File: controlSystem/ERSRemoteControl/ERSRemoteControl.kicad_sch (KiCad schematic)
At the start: 54 parts, among them J1 USB_C_Receptacle_USB2.0_14P, J2 0022-232041, J3 Conn_01x06, J4 00222-32051, J5 0022-232021, J6 0022-232021, SW1 SW_SPDT, SW2 SW_Push, SW3 SW_Push, SW4 SW_Push, SW5 SW_Push, SW6 SW_Push, SW7 SW_Push, U1 TPS63070, U2 ESP32-S3-WROOM-1, U3 TCAN330

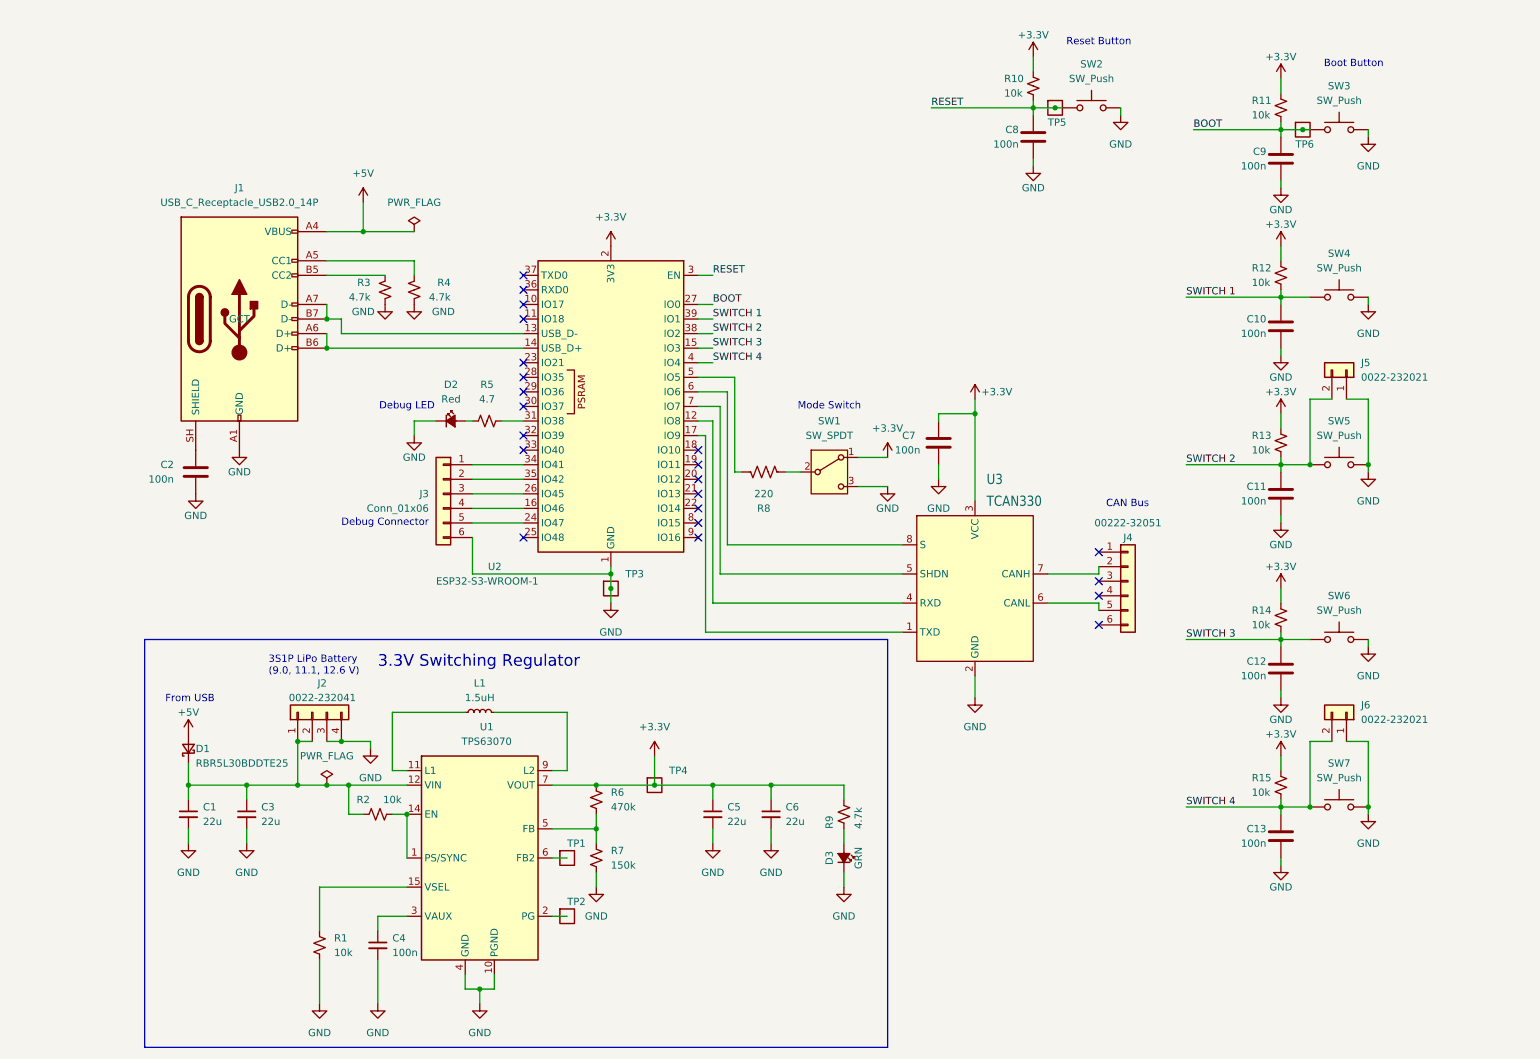
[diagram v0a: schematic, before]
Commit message: Removed CAN stuff and replaced with serial
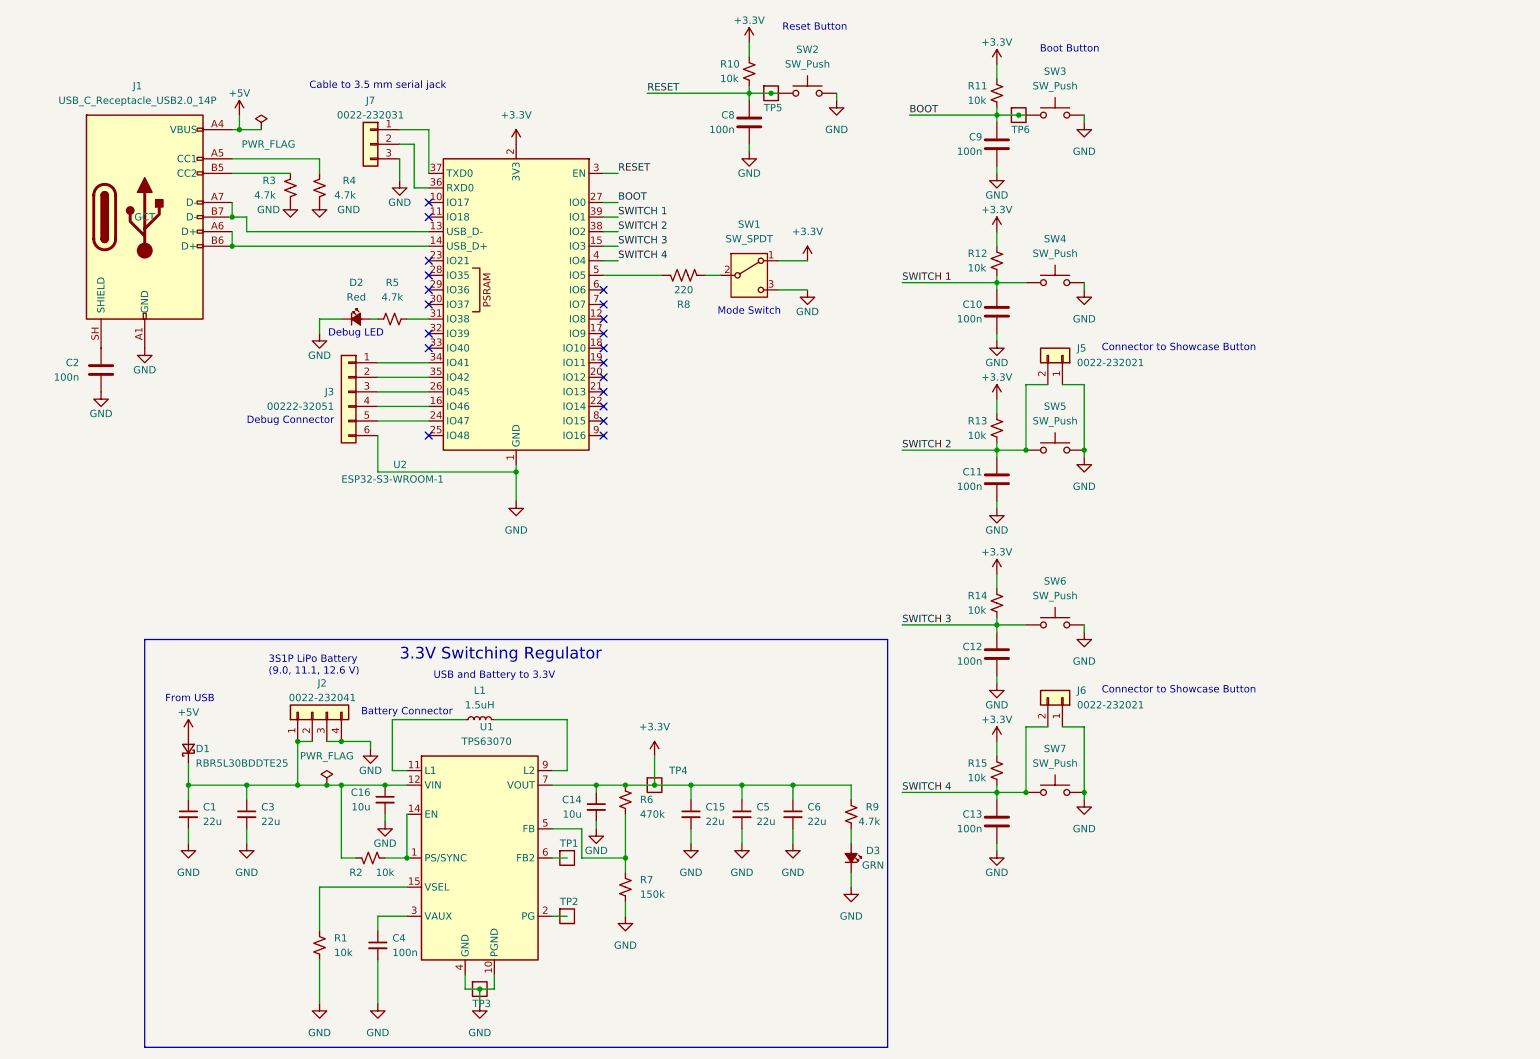
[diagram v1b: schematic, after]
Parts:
- removed C7: 100n, Capacitor_SMD:C_0603_1608Metric, symbol Device:C
- removed J4: 00222-32051, Connector_Molex:Molex_KK-254_AE-6410-06A_1x06_P2.54mm_Vertical, symbol Connector_Generic:Conn_01x06
- removed U3: TCAN330, psas-footprints:SOT23-8, symbol U-TI-TCAN330-can-transciever:TCAN330
- added C14, C16: 10u, Capacitor_SMD:C_0603_1608Metric, symbol Device:C_Small
- added C15: 22u, Capacitor_SMD:C_0805_2012Metric, symbol Device:C_Small
- added J7: 0022-232031, Connector_Molex:Molex_KK-254_AE-6410-03A_1x03_P2.54mm_Vertical, symbol Connector_Generic:Conn_01x03
- C1, C3, C5, C6: footprint Capacitor_SMD:C_0603_1608Metric -> Capacitor_SMD:C_0805_2012Metric
- D2: DPN (none) -> 732-4979-1-ND; DST (none) -> DigiKey; MFR (none) -> Wurth; MPN (none) -> 150060SS75000
- J3: value Conn_01x06 -> 00222-32051; DPN (none) -> WM4204-ND; DST (none) -> DigiKey; MFR (none) -> Molex; MPN (none) -> 22232061
- R5: value 4.7 -> 4.7k; DPN (none) -> 311-4.70KHRCT-ND; DST (none) -> DigiKey; MFR (none) -> Yageo; MPN (none) -> RC0603FR-074K7L
- R8: DPN (none) -> 311-220GRCT-ND; DST (none) -> DigiKey; MFR (none) -> Yageo; MPN (none) -> RC0603JR-07220RL
- SW1: DPN (none) -> 401-1999-1-ND; DST (none) -> DigiKey; MFR (none) -> C&K; MPN (none) -> JS102011SAQN
- SW2, SW3, SW4, SW5, SW6, SW7: DST (none) -> DigiKey; MFR Omron Electronics Inc-EMC Div -> Arata
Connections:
- net +3.3V: now also C14.1, C15.1
- net GND: now also C14.2, C15.2, C16.2, J7.3 (Pin_3)
- net at C1.1, C3.1, D1.1 (K)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: now also C16.1
- net at U2.36 (RXD0): now also J7.2 (Pin_2)
- net at U2.37 (TXD0): now also J7.1 (Pin_1)
- no-connect marks 22 -> 20
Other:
- note added: "Battery Connector"
- note added: "Cable to 3.5 mm serial jack"
- note added: "Connector to Showcase Button"
- note added: "USB and Battery to 3.3V"
- note removed: "CAN Bus"
- moved on the sheet: C10, C11, C12, C13, C2, C5, C6, C8, C9, D2, D3, J1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

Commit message: More changes to layout to make it cleaner
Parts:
- removed J3: 00222-32051, Connector_Molex:Molex_KK-254_AE-6410-06A_1x06_P2.54mm_Vertical, symbol Connector_Generic:Conn_01x06
- added TP7, TP8: Test-Point, psas-footprints:TP-through-hole-1X01, symbol psas-testpoint:Test-Point
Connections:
- net at U2.34 (IO41): now also TP7.1
- net at U2.35 (IO42): now also TP8.1
- no-connect marks 20 -> 19
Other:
- note removed: "Debug Connector"

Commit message: Replaced components in BOM
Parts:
- C1, C15, C3, C5, C6: DPN 445-14428-1-ND -> 490-GRT21BC81C226ME13LCT-ND; MPN C2012X5R1V226M125AC -> GRT21BC81C226ME13L
- C14, C16: footprint Capacitor_SMD:C_0603_1608Metric -> Capacitor_SMD:C_0805_2012Metric; DPN 445-14428-1-ND -> 490-GRT21BC71E106KE13KCT-ND; MPN C2012X5R1V226M125AC -> GRT21BC71E106KE13K
- R3, R4, R5, R9: DPN 311-4.70KHRCT-ND -> RMCF0603FT4K70CT-ND; MFR Yageo -> Stackpole Electronics Inc.; MPN RC0603FR-074K7L -> RMCF0603FT4K70
- R6: DPN 311-470KHRCT-ND -> RMCF0603FT470KCT-ND; MFR Yageo -> Stackpole Electronics Inc.; MPN RC0603FR-07470KL -> RMCF0603FT470K
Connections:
- no-connect marks 19 -> 23
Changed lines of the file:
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@@
 	)
 	(no_connect
+		(at 87.63 86.36)
+	)
+	(no_connect
 		(at 118.11 60.96)
 	)
@@
 	)
 	(no_connect
+		(at 87.63 83.82)
+	)
+	(no_connect
 		(at 118.11 66.04)
 	)
@@
 	)
 	(no_connect
+		(at 87.63 78.74)
+	)
+	(no_connect
 		(at 87.63 68.58)
 	)
@@
 	)
 	(no_connect
+		(at 87.63 81.28)
+	)
+	(no_connect
 		(at 87.63 45.72)
 	)
@@
 			)
 		)
-		(property "DPN" "311-470KHRCT-ND"
+		(property "DPN" "RMCF0603FT470KCT-ND"
 			(at 121.92 149.86 0)
 			(hide yes)
@@
 			)
 		)
-		(property "MFR" "Yageo"
+		(property "MFR" "Stackpole Electronics Inc."
 			(at 121.92 149.86 0)
 			(hide yes)
@@
 			)
 		)
-		(property "MPN" "RC0603FR-07470KL"
+		(property "MPN" "RMCF0603FT470K"
 			(at 121.92 149.86 0)
 			(hide yes)
@@
 			)
 		)
-		(property "MFR" "Yageo"
+		(property "MFR" "Stackpole Electronics Inc."
 			(at 81.28 66.04 90)
 			(hide yes)
@@
 			)
 		)
-		(property "MPN" "RC0603FR-074K7L"
+		(property "MPN" "RMCF0603FT4K70"
 			(at 81.28 66.04 90)
 			(hide yes)
@@
 			)
 		)
-		(property "DPN" "311-4.70KHRCT-ND"
+		(property "DPN" "RMCF0603FT4K70CT-ND"
 			(at 81.28 66.04 90)
 			(hide yes)
@@
 			)
 		)
-		(property "MFR" "Yageo"
+		(property "MFR" "Stackpole Electronics Inc."
 			(at 63.5 43.18 0)
 			(hide yes)
@@
 			)
 		)
-		(property "MPN" "RC0603FR-074K7L"
+		(property "MPN" "RMCF0603FT4K70"
 			(at 63.5 43.18 0)
 			(hide yes)
@@
 			)
 		)
-		(property "DPN" "311-4.70KHRCT-ND"
+		(property "DPN" "RMCF0603FT4K70CT-ND"
 			(at 63.5 43.18 0)
 			(hide yes)
@@
 			)
 		)
-		(property "DPN" "445-14428-1-ND"
+		(property "DPN" "490-GRT21BC81C226ME13LCT-ND"
 			(at 55.88 152.4 0)
 			(hide yes)
@@
 			)
 		)
-		(property "MPN" "C2012X5R1V226M125AC"
+		(property "MPN" "GRT21BC81C226ME13L"
 			(at 55.88 152.4 0)
 			(hide yes)
@@
 			)
 		)
-		(property "MPN" "C2012X5R1V226M125AC"
+		(property "MPN" "GRT21BC81C226ME13L"
 			(at 142.24 152.4 0)
 			(hide yes)
@@
 			)
 		)
-		(property "DPN" "445-14428-1-ND"
+		(property "DPN" "490-GRT21BC81C226ME13LCT-ND"
 			(at 142.24 152.4 0)
 			(hide yes)
@@
 			)
 		)
-		(property "DPN" "311-4.70KHRCT-ND"
+		(property "DPN" "RMCF0603FT4K70CT-ND"
 			(at 161.29 152.4 0)
 			(hide yes)
@@
 			)
 		)
-		(property "MFR" "Yageo"
+		(property "MFR" "Stackpole Electronics Inc."
 			(at 161.29 152.4 0)
 			(hide yes)
@@
 			)
 		)
-		(property "MPN" "RC0603FR-074K7L"
+		(property "MPN" "RMCF0603FT4K70"
 			(at 161.29 152.4 0)
 			(hide yes)
@@
 			)
 		)
-		(property "MPN" "C2012X5R1V226M125AC"
+		(property "MPN" "GRT21BC81C226ME13L"
 			(at 151.13 152.4 0)
 			(hide yes)
@@
 			)
 		)
-		(property "DPN" "445-14428-1-ND"
+		(property "DPN" "490-GRT21BC81C226ME13LCT-ND"
 			(at 151.13 152.4 0)
 			(hide yes)
@@
 			)
 		)
-		(property "MFR" "Yageo"
+		(property "MFR" "Stackpole Electronics Inc."
 			(at 68.58 43.18 0)
 			(hide yes)
@@
 			)
 		)
-		(property "MPN" "RC0603FR-074K7L"
+		(property "MPN" "RMCF0603FT4K70"
 			(at 68.58 43.18 0)
 			(hide yes)
@@
 			)
 		)
-		(property "DPN" "311-4.70KHRCT-ND"
+		(property "DPN" "RMCF0603FT4K70CT-ND"
 			(at 68.58 43.18 0)
 			(hide yes)
@@
 			)
 		)
-		(property "DPN" "445-14428-1-ND"
+		(property "DPN" "490-GRT21BC81C226ME13LCT-ND"
 			(at 45.72 152.4 0)
 			(hide yes)
@@
 			)
 		)
-		(property "MPN" "C2012X5R1V226M125AC"
+		(property "MPN" "GRT21BC81C226ME13L"
 			(at 45.72 152.4 0)
 			(hide yes)
@@
 			)
 		)
-		(property "Footprint" "Capacitor_SMD:C_0603_1608Metric"
+		(property "Footprint" "Capacitor_SMD:C_0805_2012Metric"
 			(at 80.01 149.86 0)
 			(hide yes)
@@
 			)
 		)
-		(property "MPN" "C2012X5R1V226M125AC"
+		(property "MPN" "GRT21BC71E106KE13K"
 			(at 80.01 149.86 0)
 			(hide yes)
@@
 			)
 		)
-		(property "DPN" "445-14428-1-ND"
+		(property "DPN" "490-GRT21BC71E106KE13KCT-ND"
 			(at 80.01 149.86 0)
 			(hide yes)
@@
 			)
 		)
-		(property "MPN" "C2012X5R1V226M125AC"
+		(property "MPN" "GRT21BC81C226ME13L"
 			(at 133.35 152.4 0)
 			(hide yes)
@@
 			)
 		)
-		(property "DPN" "445-14428-1-ND"
+		(property "DPN" "490-GRT21BC81C226ME13LCT-ND"
 			(at 133.35 152.4 0)
 			(hide yes)
@@
 			)
 		)
-		(property "Footprint" "Capacitor_SMD:C_0603_1608Metric"
+		(property "Footprint" "Capacitor_SMD:C_0805_2012Metric"
 			(at 116.84 151.13 0)
 			(hide yes)
@@
 			)
 		)
-		(property "MPN" "C2012X5R1V226M125AC"
+		(property "MPN" "GRT21BC71E106KE13K"
 			(at 116.84 151.13 0)
 			(hide yes)
@@
 			)
 		)
-		(property "DPN" "445-14428-1-ND"
+		(property "DPN" "490-GRT21BC71E106KE13KCT-ND"
 			(at 116.84 151.13 0)
 			(hide yes)

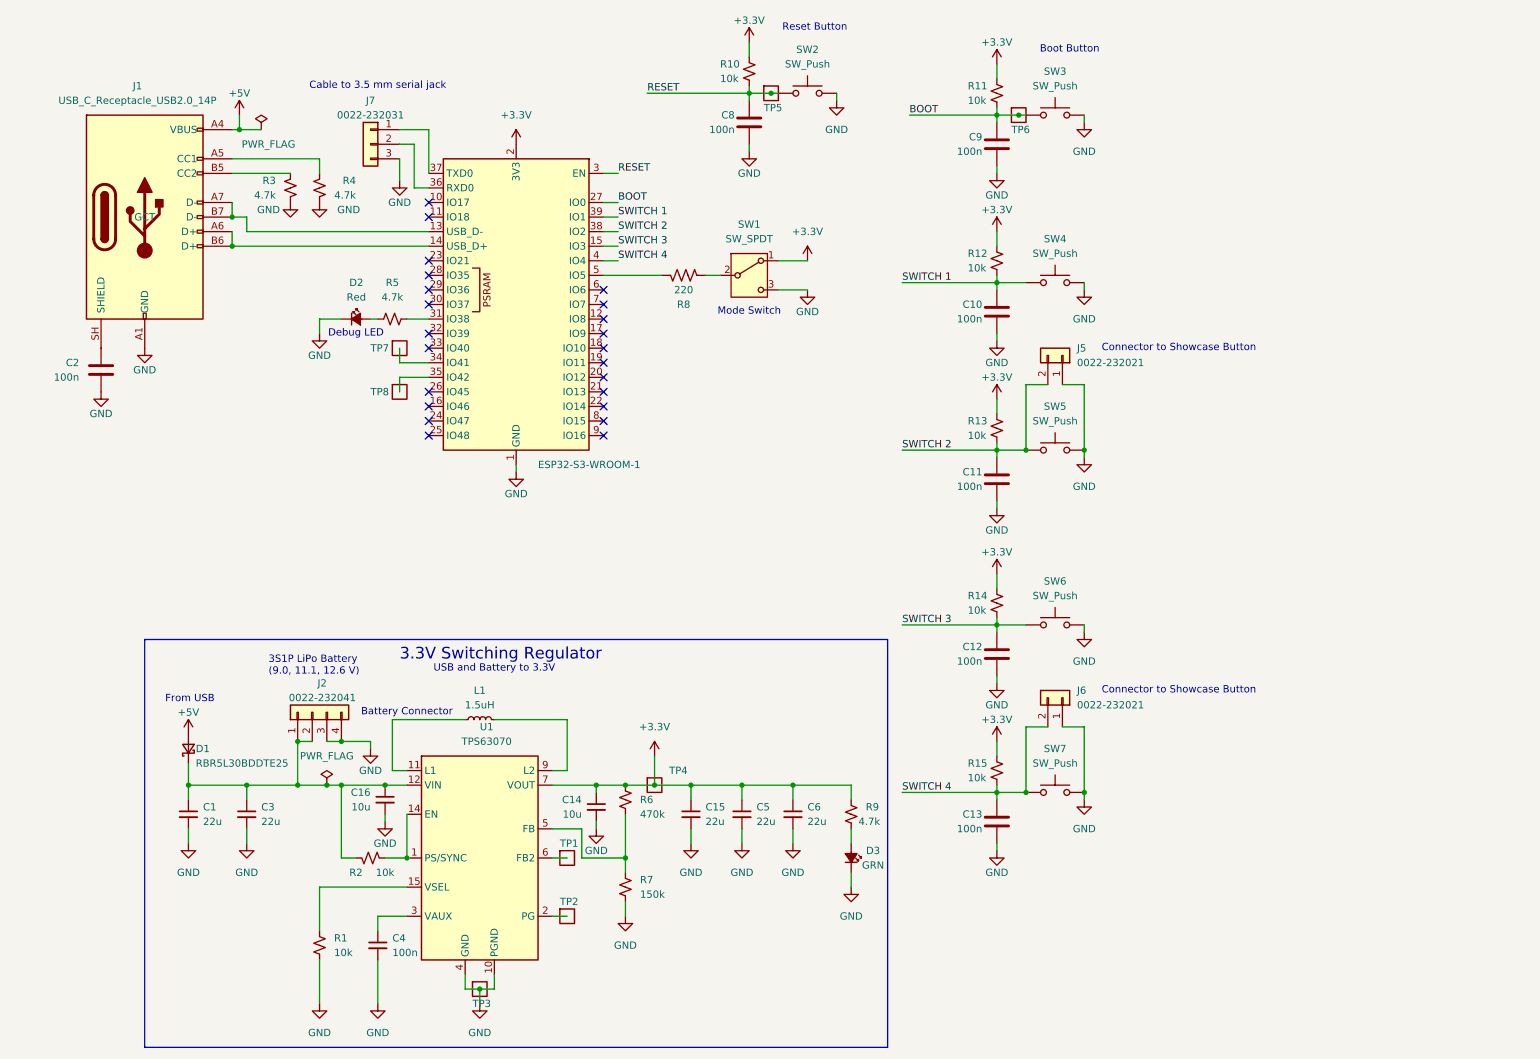
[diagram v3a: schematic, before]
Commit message: Removed mode switch cleaned up traces, minimum trace size to .3 mm
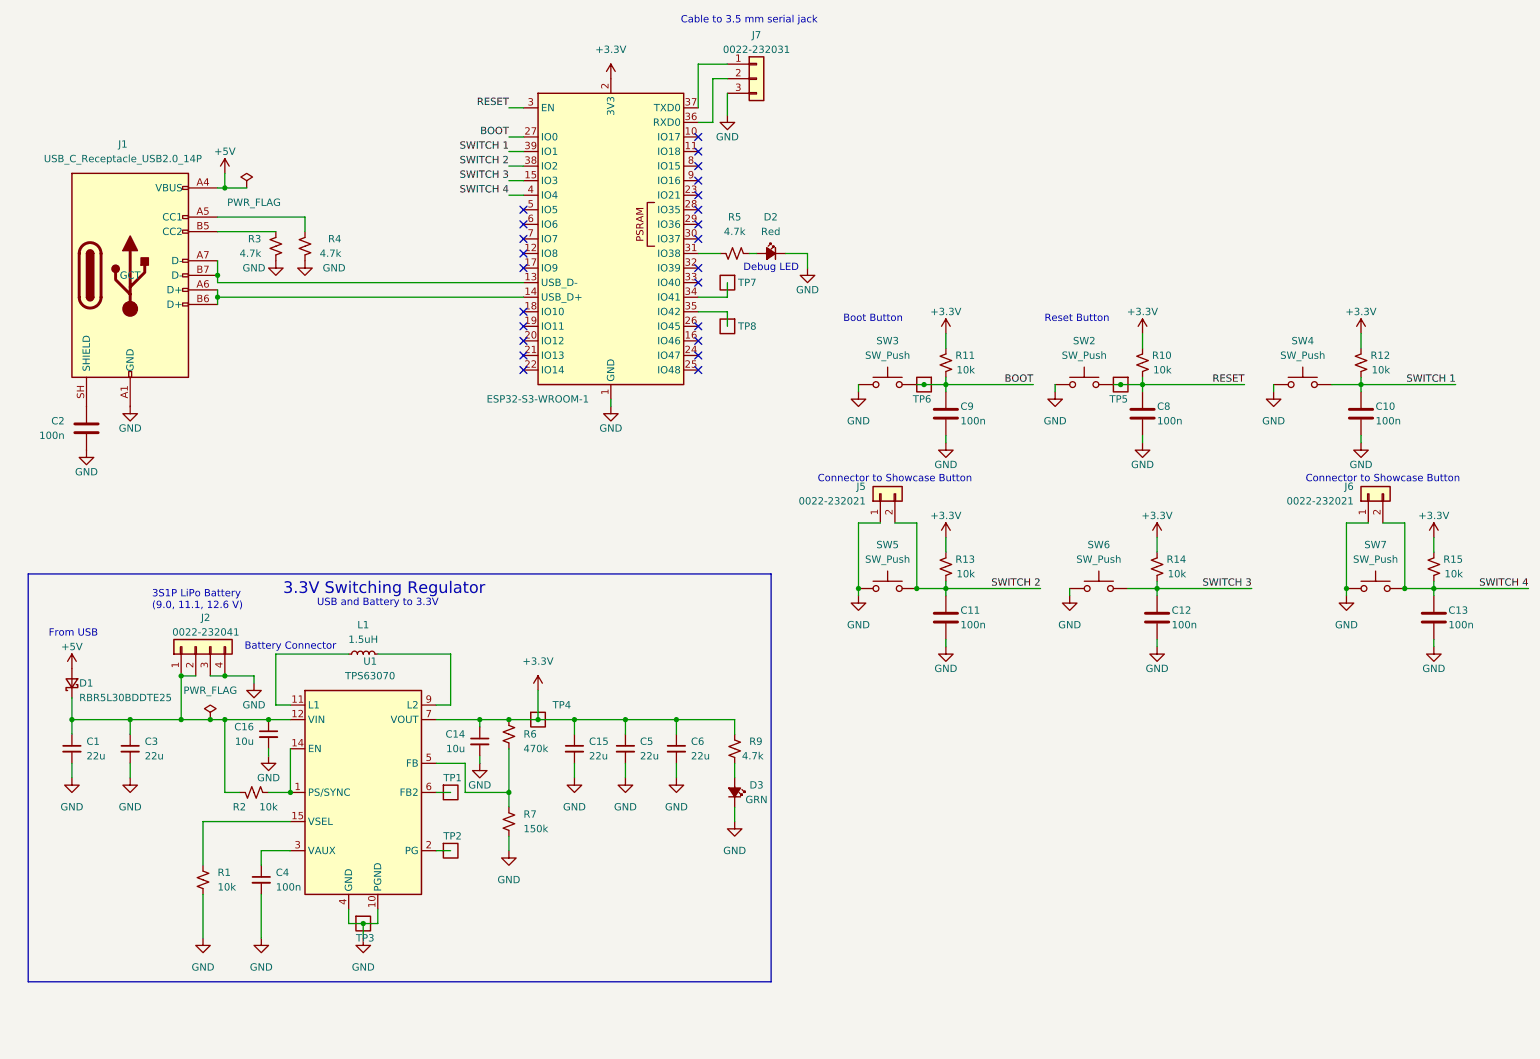
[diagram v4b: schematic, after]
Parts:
- removed R8: 220, Resistor_SMD:R_0603_1608Metric, symbol Device:R_US
- removed SW1: SW_SPDT, Button_Switch_SMD:SW_SPDT_CK_JS102011SAQN, symbol Switch:SW_SPDT
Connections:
- no-connect marks 23 -> 24
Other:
- note removed: "Mode Switch"
- moved on the sheet: C1, C10, C11, C12, C13, C14, C15, C16, C2, C3, C4, C5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
